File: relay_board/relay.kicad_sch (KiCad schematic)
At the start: 34 parts, among them J2 ACT_PWR, J3 ACT_PWR, J4 Actuator, K1 PS2702-1-F3-A, K2 PS2702-1-F3-A, K3 T9GV1L14-12, U7 INA180A3, U8 INA180A3

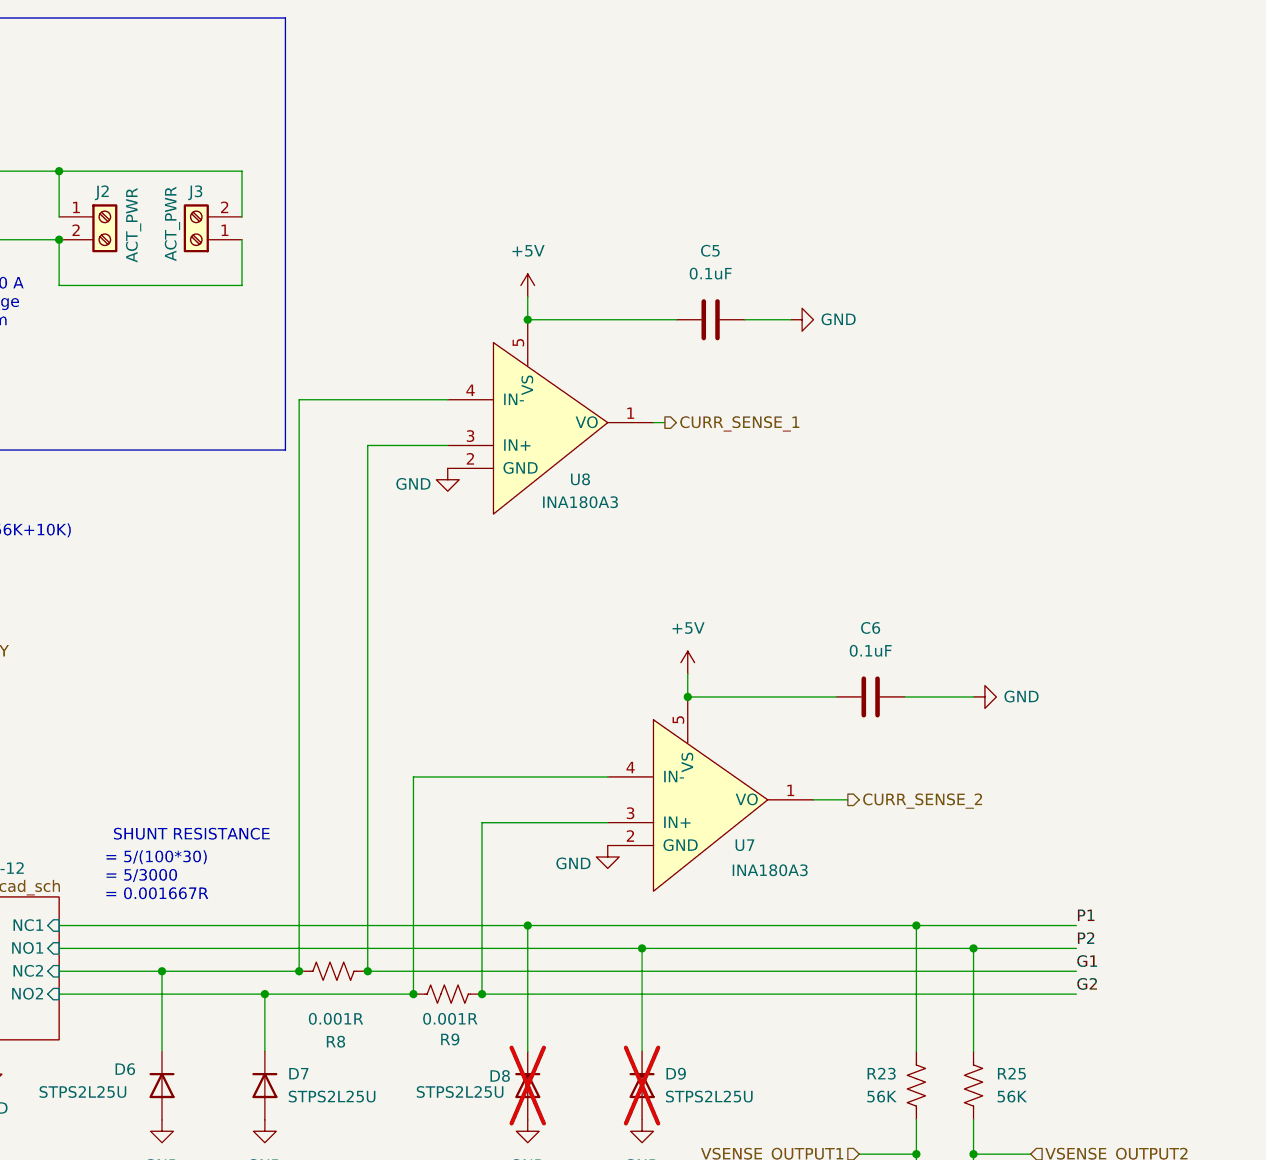
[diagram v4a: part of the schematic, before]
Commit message: lowpass current sense; move power traces to FCu
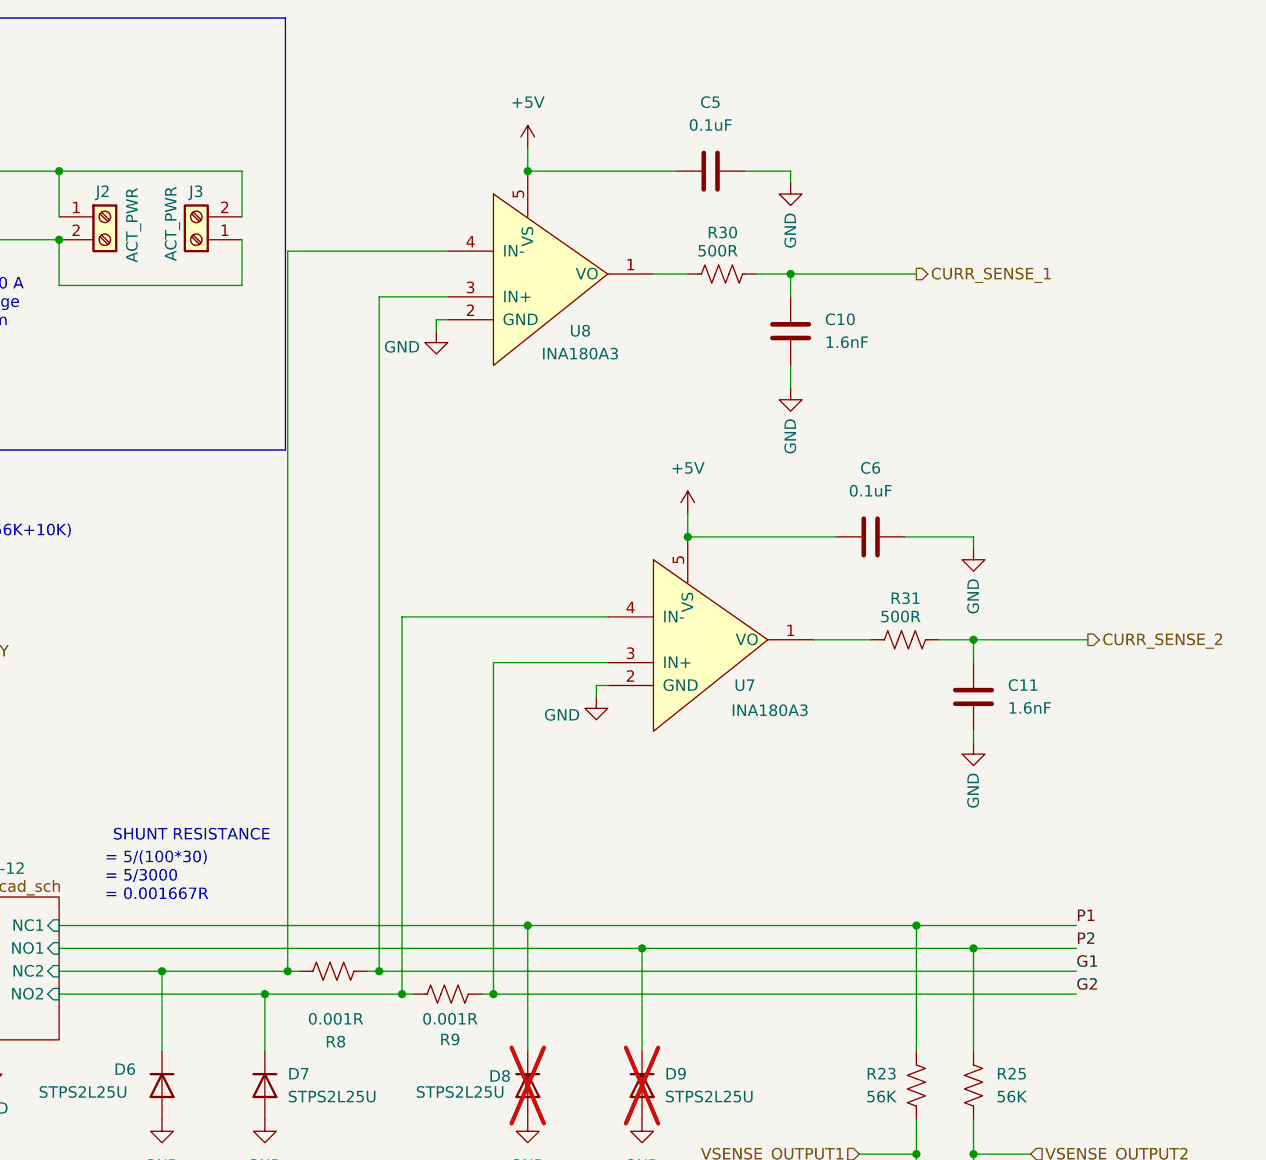
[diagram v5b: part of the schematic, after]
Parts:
- added C10, C11: 1.6nF, Capacitor_SMD:C_0805_2012Metric_Pad1.18x1.45mm_HandSolder, symbol Device:C
- added R30, R31: 500R, Resistor_SMD:R_0805_2012Metric_Pad1.20x1.40mm_HandSolder, symbol Device:R_US
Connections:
- net CURR_SENSE_1: now also C10.2, R30.1; no longer U8.1 (VO)
- net CURR_SENSE_2: now also C11.2, R31.1; no longer U7.1 (VO)
- net GND: now also C10.1, C11.1
- new net: R30.2, U8.1 (VO)
- new net: R31.2, U7.1 (VO)
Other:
- moved on the sheet: C5, C6, U7, U8
